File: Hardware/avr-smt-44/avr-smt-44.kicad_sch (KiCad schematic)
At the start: 20 parts, among them J1 AVR-ISP-6, SW1 SW_Push, U1 ATtiny84A-SS

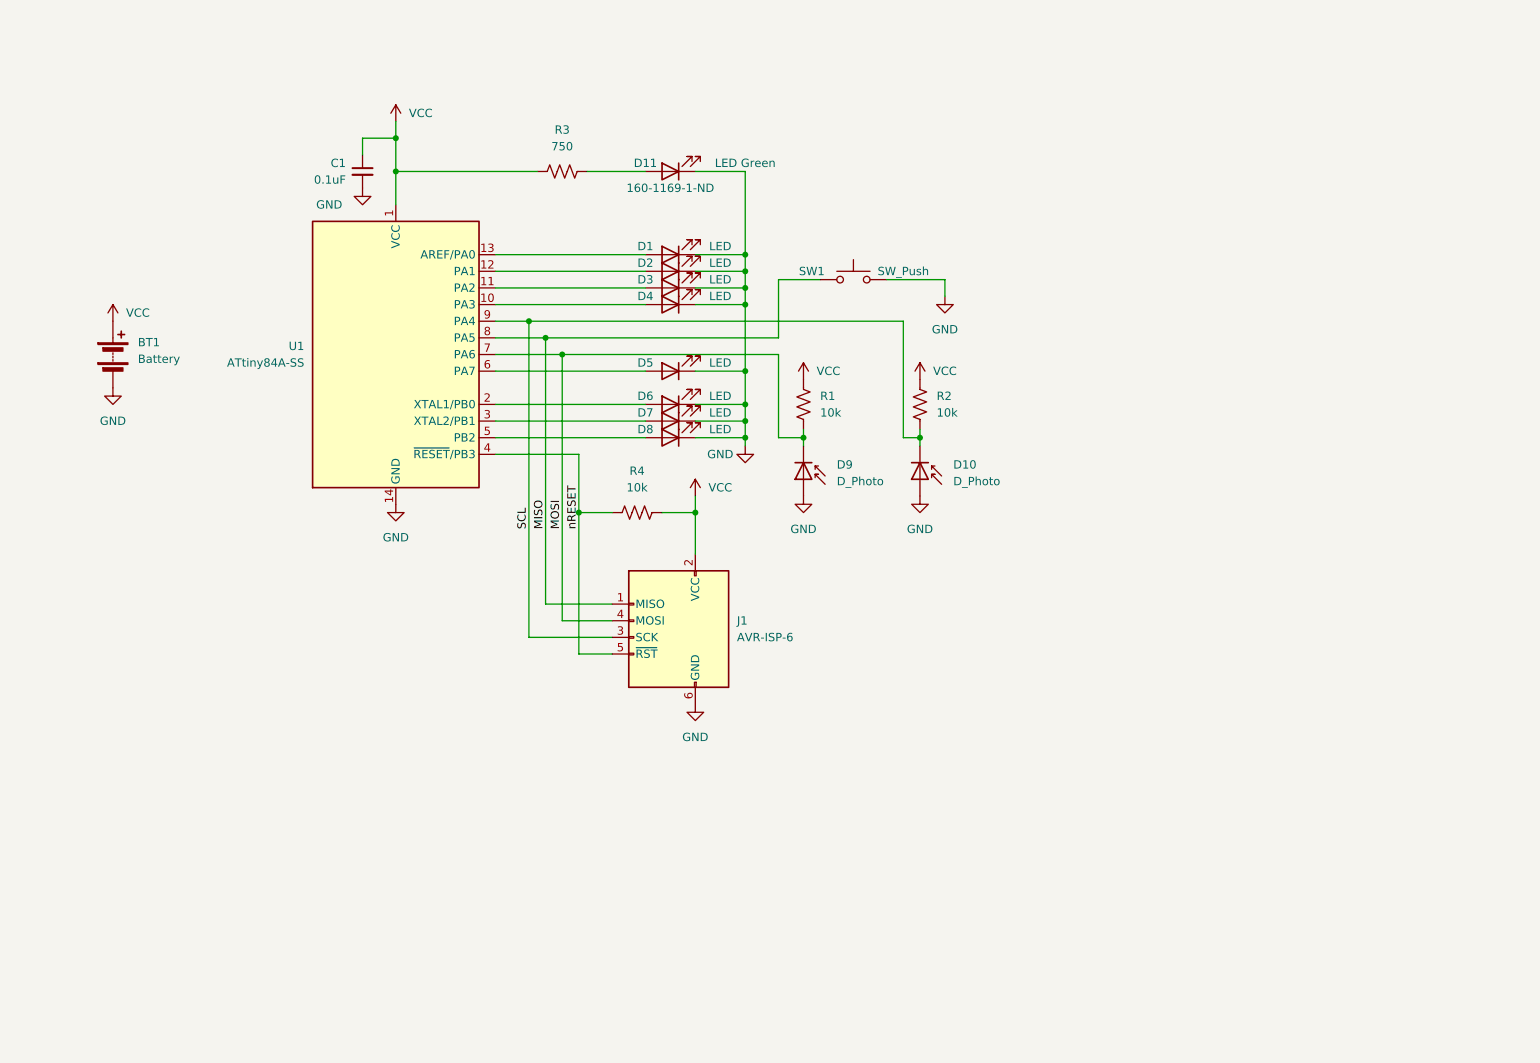
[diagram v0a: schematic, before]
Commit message: Add series R, re-place
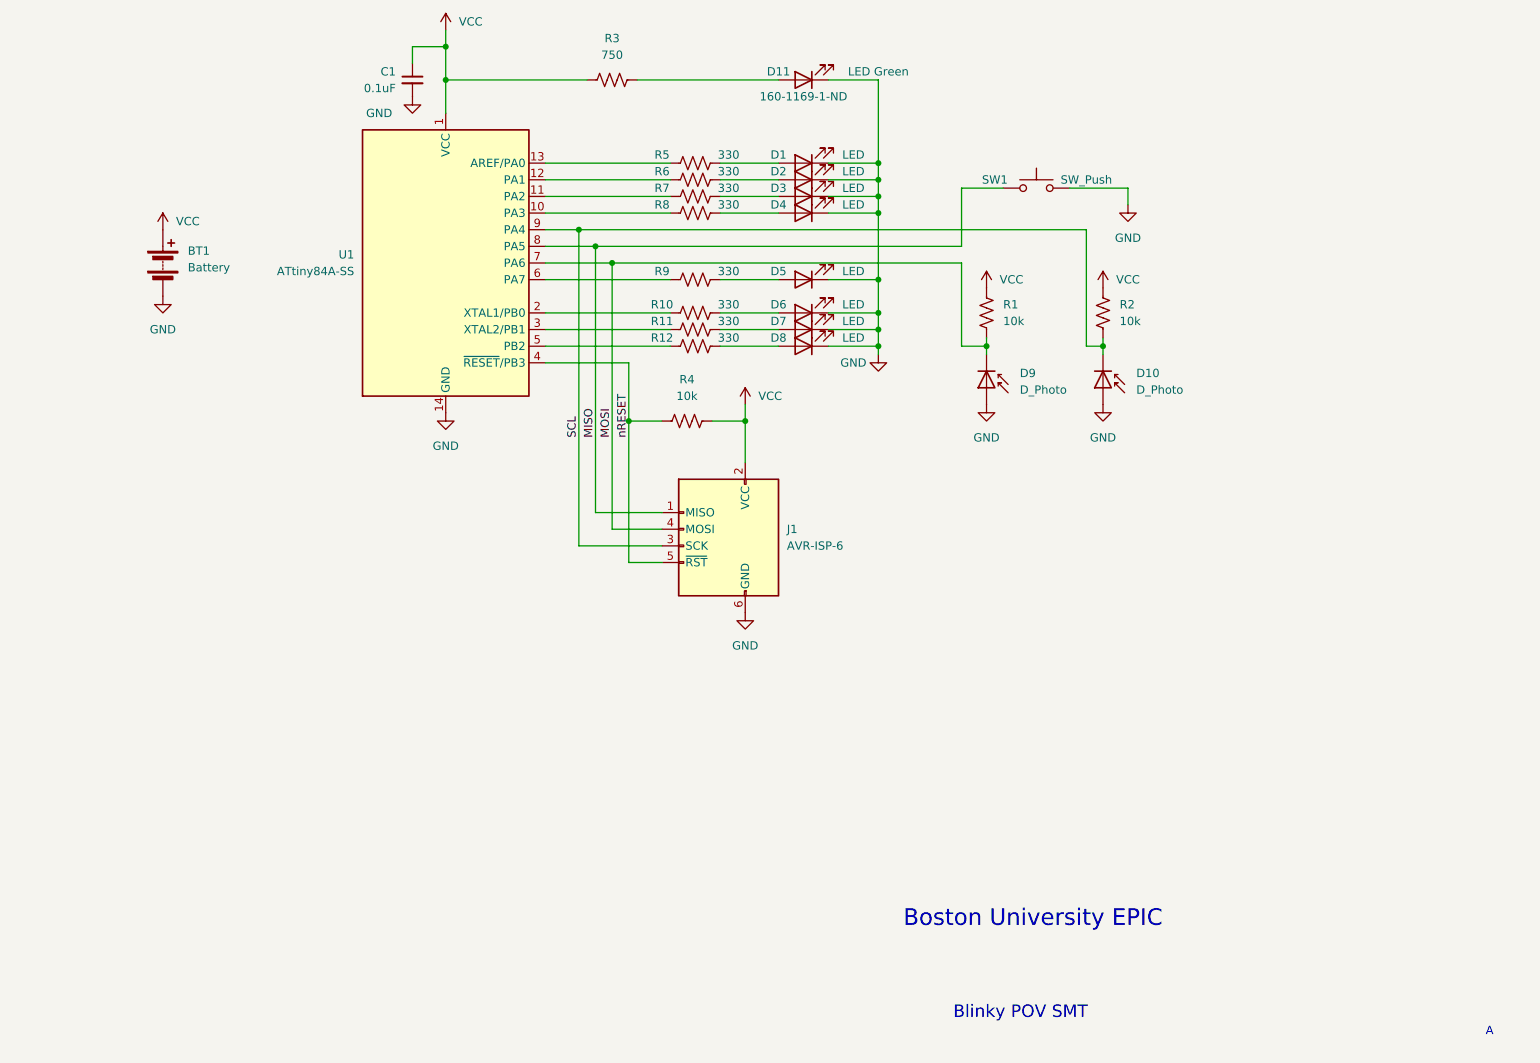
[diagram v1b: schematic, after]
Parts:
- added R10, R11, R12, R5, R6, R7, R8, R9: 330, Resistor_SMD:R_1206_3216Metric_Pad1.30x1.75mm_HandSolder, symbol Device:R_US
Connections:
- net at U1.2 (XTAL1/PB0): now also R10.1; no longer D6.2 (A)
- net at D3.2 (A): now also R7.2; no longer U1.11 (PA2)
- net at D4.2 (A): now also R8.2; no longer U1.10 (PA3)
- net at U1.12 (PA1): now also R6.1; no longer D2.2 (A)
- net at U1.13 (AREF/PA0): now also R5.1; no longer D1.2 (A)
- net at U1.3 (XTAL2/PB1): now also R11.1; no longer D7.2 (A)
- net at U1.5 (PB2): now also R12.1; no longer D8.2 (A)
- net at U1.6 (PA7): now also R9.1; no longer D5.2 (A)
- new net: D6.2 (A), R10.2
- new net: D2.2 (A), R6.2
- new net: D5.2 (A), R9.2
- new net: R7.1, U1.11 (PA2)
- new net: D8.2 (A), R12.2
- new net: R8.1, U1.10 (PA3)
- new net: D7.2 (A), R11.2
- new net: D1.2 (A), R5.2
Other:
- note added: "A"
- note added: "Blinky POV SMT"
- note added: "Boston University EPIC"
- moved on the sheet: BT1, C1, D1, D10, D11, D2, D3, D4, D5, D6, D7, D8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

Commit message: V5 for submit
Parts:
- added N1: Housing, rhett_logo:rhett_logo, symbol Mechanical:Housing
- added TP1, TP2: TestPoint, TestPoint:TestPoint_Loop_D3.80mm_Drill2.0mm, symbol Connector:TestPoint
- BT1: CatNo (none) -> 1568-1408-ND
- C1: CatNo (none) -> 399-C1206C104K3RAC7800CT-ND
- D1, D2, D3, D4, D5, D6, D7, D8: CatNo (none) -> 3147-T1341USD-30C000112U1930CT-ND
- D10, D9: CatNo (none) -> 751-1057-ND
- J1: CatNo (none) -> 10129383-906002BLF-ND
- R1, R2, R4: CatNo (none) -> 311-10KERCT-ND
- R10, R11, R12, R5, R6, R7, R8, R9: CatNo (none) -> 311-330ERCT-ND
- R3: CatNo (none) -> 311-750ERCT-ND
- SW1: CatNo (none) -> SW400-ND
- U1: CatNo (none) -> ATTINY84A-SSURCT-ND
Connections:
- net GND: now also TP1.1, TP2.1

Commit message: V5.1 PCB, notes
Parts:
- J1: footprint Connector_PinHeader_2.54mm:PinHeader_2x03_P2.54mm_Vertical_SMD -> Connector_PinHeader_2.54mm:PinHeader_2x03_P2.54mm_Vertical; CatNo 10129383-906002BLF-ND -> 10129381-906002BLF-ND
- N1: value Housing -> Rhett Logo
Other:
- note added: "5.1"
- note added: "Rev 5.1 - change J1 to TH - increase zone thermal relief"
- note removed: "A"
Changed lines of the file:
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@@
     (stroke (width 0) (type default))
   )
-  (text "A" (at 252.73 199.39 0)
-    (effects (font (size 1.27 1.27)) (justify left bottom))
+  (text "Rev 5.1 \n- change J1 to TH\n- increase zone thermal relief"
+    (at 27.94 177.8 0)
+    (effects (font (size 1.905 1.905)) (justify left bottom))
+  )
+  (text "5.1" (at 252.73 200.66 0)
+    (effects (font (size 1.905 1.905)) (justify left bottom))
   )
   (text "Boston University EPIC" (at 163.83 182.88 0)
@@
       (effects (font (size 1.27 1.27)) (justify left))
     )
-    (property "Value" "Housing" (at 50.8 105.7275 0)
+    (property "Value" "Rhett Logo" (at 50.8 105.7275 0)
       (effects (font (size 1.27 1.27)) (justify left))
     )
@@
       (effects (font (size 1.27 1.27)) (justify right))
     )
-    (property "Footprint" "Connector_PinHeader_2.54mm:PinHeader_2x03_P2.54mm_Vertical_SMD" (at 143.51 123.19 90)
+    (property "Footprint" "Connector_PinHeader_2.54mm:PinHeader_2x03_P2.54mm_Vertical" (at 143.51 123.19 90)
       (effects (font (size 1.27 1.27)) hide)
     )
@@
       (effects (font (size 1.27 1.27)) hide)
     )
-    (property "CatNo" "10129383-906002BLF-ND" (at 158.75 127 0)
-      (effects (font (size 1.27 1.27)))
-    )
+    (property "CatNo" "10129381-906002BLF-ND" (at 158.75 127 0)
+      (effects (font (size 1.27 1.27)))
+    )

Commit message: V5.1 as built
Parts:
- N1, TP1, TP2: now left out of the parts list
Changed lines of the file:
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@@
   )
   (symbol (lib_id "Connector:TestPoint") (at 67.31 132.08 0) (unit 1)
-    (in_bom yes) (on_board yes) (dnp no) (fields_autoplaced)
+    (in_bom no) (on_board yes) (dnp no) (fields_autoplaced)
     (property "Reference" "TP2" (at 69.85 127.508 0)
       (effects (font (size 1.27 1.27)) (justify left))
@@
   )
   (symbol (lib_id "Connector:TestPoint") (at 50.8 132.08 0) (unit 1)
-    (in_bom yes) (on_board yes) (dnp no) (fields_autoplaced)
+    (in_bom no) (on_board yes) (dnp no) (fields_autoplaced)
     (property "Reference" "TP1" (at 53.34 127.508 0)
       (effects (font (size 1.27 1.27)) (justify left))
@@
   )
   (symbol (lib_id "Mechanical:Housing") (at 46.99 104.14 0) (unit 1)
-    (in_bom yes) (on_board yes) (dnp no) (fields_autoplaced)
+    (in_bom no) (on_board yes) (dnp no) (fields_autoplaced)
     (property "Reference" "N1" (at 50.8 103.1875 0)
       (effects (font (size 1.27 1.27)) (justify left))

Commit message: updated instructions and assy dwg for 2/12 class
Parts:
- J1: now not fitted
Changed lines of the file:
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@@
   )
   (symbol (lib_id "Connector:AVR-ISP-6") (at 137.16 124.46 0) (mirror y) (unit 1)
-    (in_bom yes) (on_board yes) (dnp no)
+    (in_bom yes) (on_board yes) (dnp yes)
     (property "Reference" "J1" (at 146.05 121.92 0)
       (effects (font (size 1.27 1.27)) (justify right))
